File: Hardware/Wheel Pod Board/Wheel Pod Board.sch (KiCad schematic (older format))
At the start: 1 part, among them U1 STM32F401RCT6

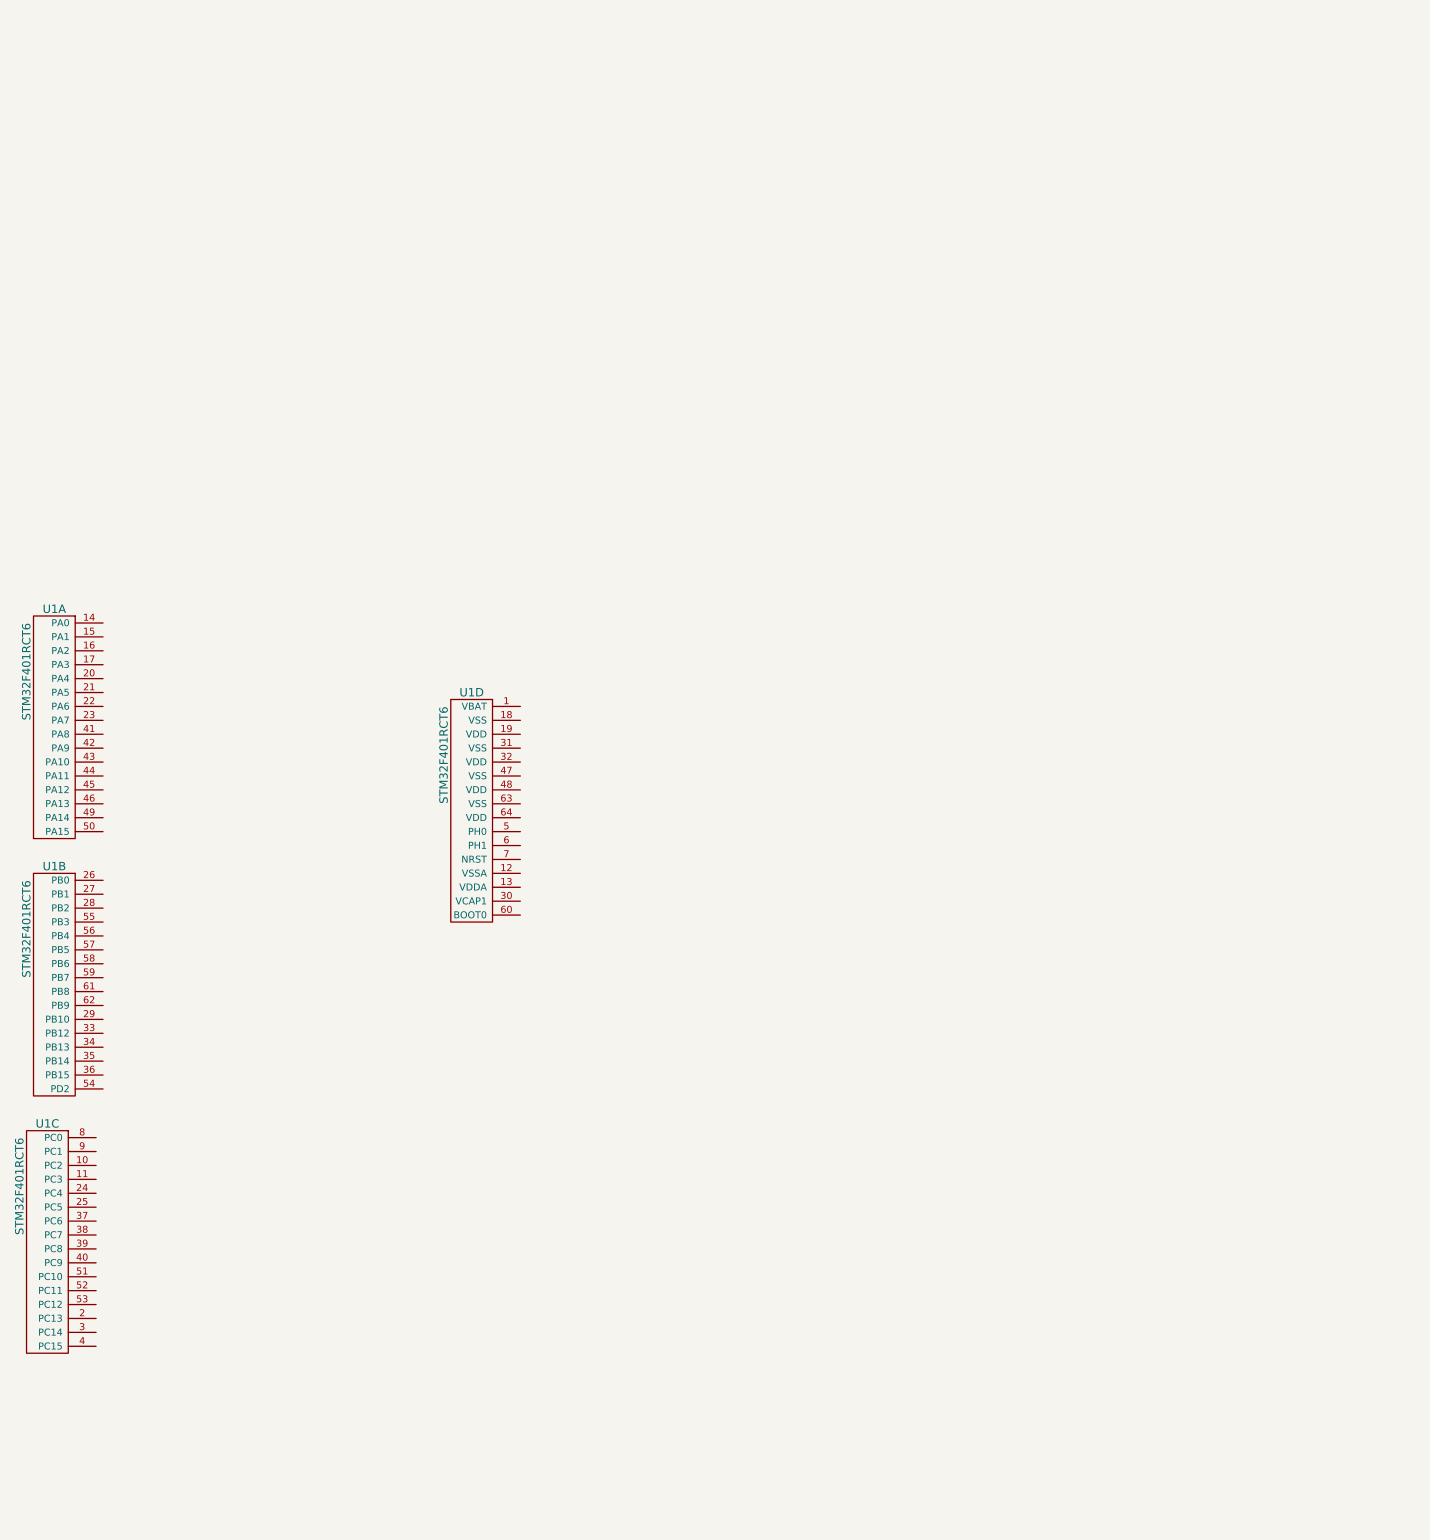
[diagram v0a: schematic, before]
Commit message: Import common blocks from Arm Board
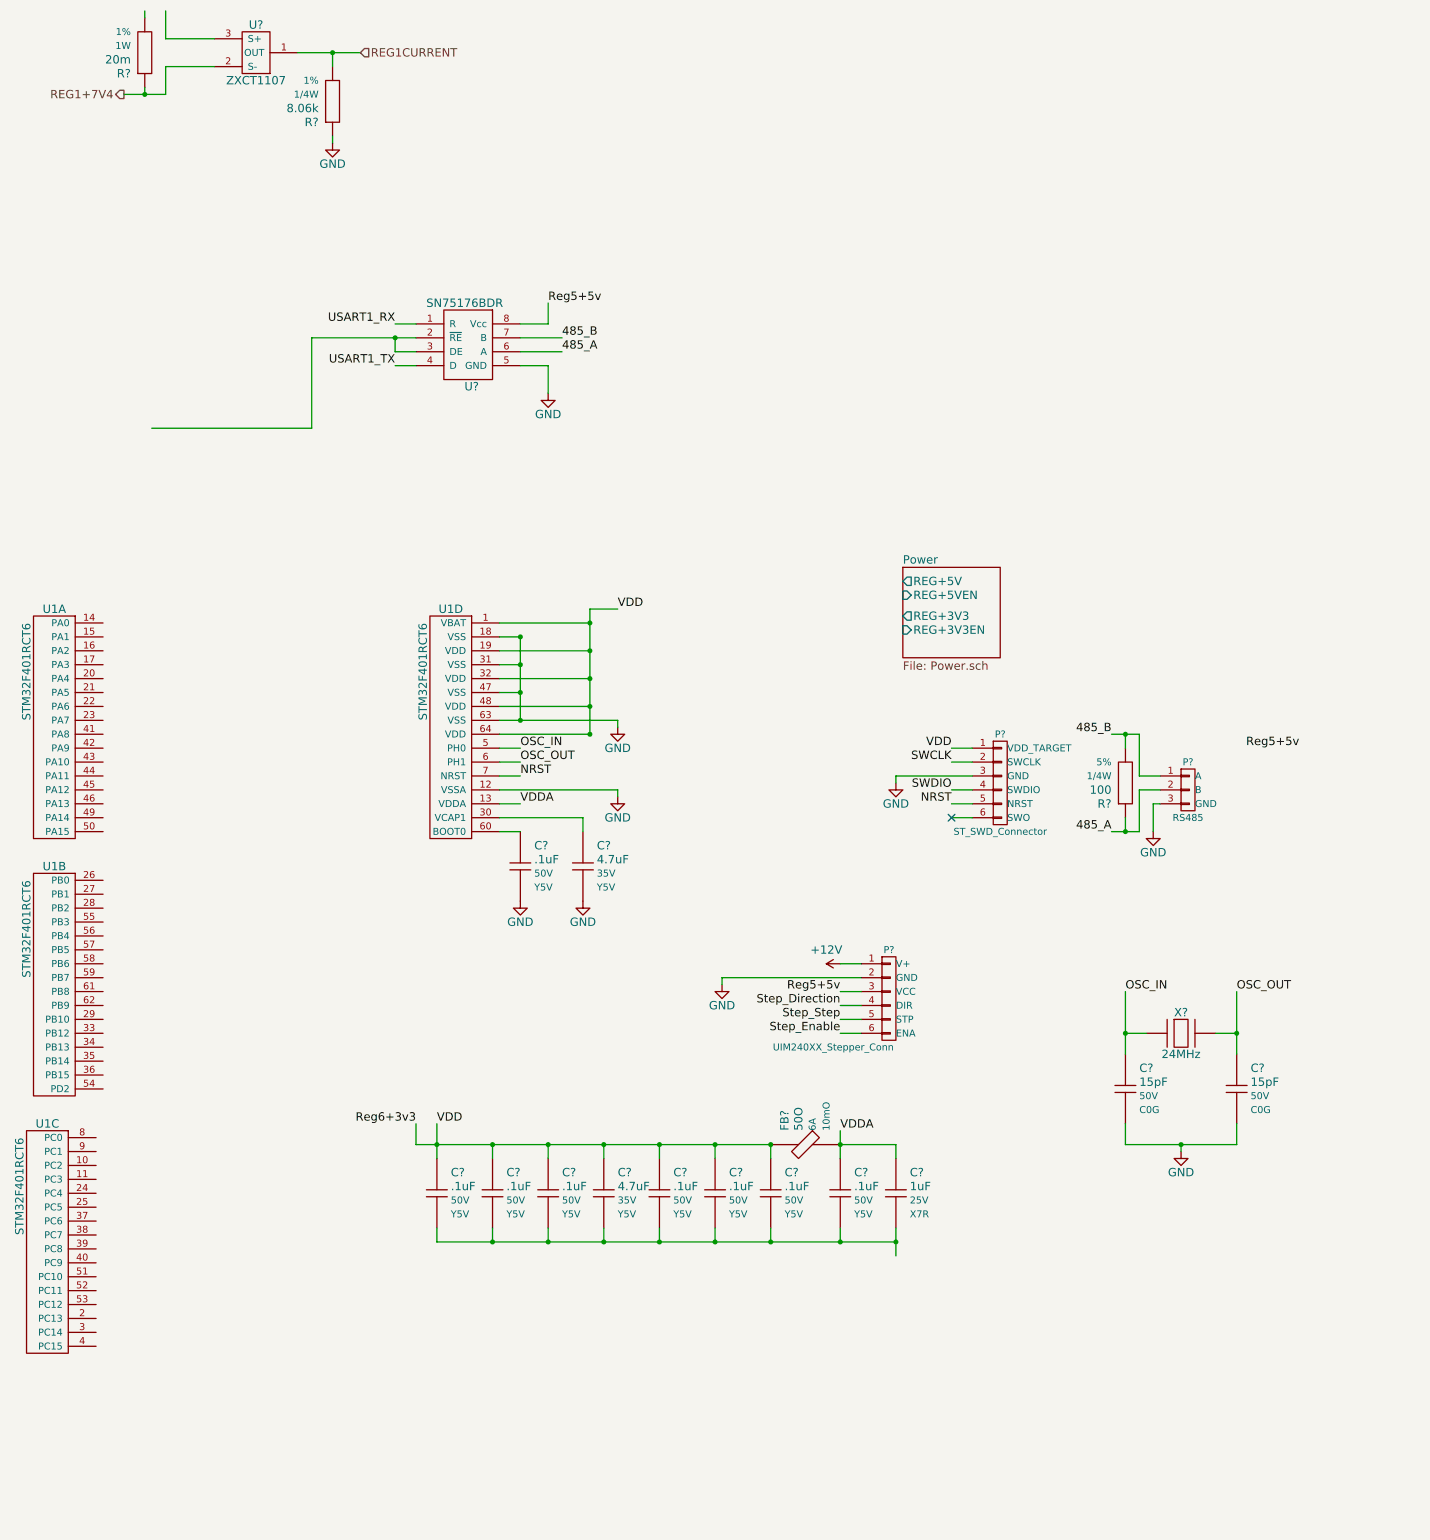
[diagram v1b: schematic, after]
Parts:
- added C? (x2): 4.7uF, Capacitors_SMD:C_1206_HandSoldering, symbol Capacitor
- added C? (x8): .1uF, Capacitors_SMD:C_1206_HandSoldering, symbol Capacitor
- added C?: 1uF, Capacitors_SMD:C_1206_HandSoldering, symbol Capacitor
- added C? (x2): 15pF, Capacitors_SMD:C_1206_HandSoldering, symbol Capacitor
- added FB?: 50O, Resistors_SMD:R_1206_HandSoldering, symbol Ferrite
- added P?: UIM240XX_Stepper_Conn, MAVRIC_footprints:1x6_SMD_header, symbol UIM240XX_Conn
- added P?: RS485, MAVRIC_footprints:1x3_SMD_header, symbol RS485
- added P?: ST_SWD_Connector, MAVRIC_footprints:1x6_SMD_header, symbol ST_SWD_Connector
- added R?: 20m, Resistors_SMD:R_1206_HandSoldering, symbol Resistor
- added R?: 8.06k, Resistors_SMD:R_1206_HandSoldering, symbol Resistor
- added R?: 100, Resistors_SMD:R_1206_HandSoldering, symbol Resistor
- added U?: SN75176BDR, SMD_Packages:SOIC-8-W, symbol SN75176BDR
- added U?: ZXCT1107, Housings_SOT-23_SOT-143_TSOT-6:SOT23_Transistor_Handsoldering_RevB_14Mar2014, symbol ZXCT1107
- added X?: 24MHz, Crystals_Oscillators_SMD:Q_49U3HMS, symbol Crystal
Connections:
- net labels added: +12V, 485_A, 485_B, GND, NRST, OSC_IN, OSC_OUT, REG1+7V4, REG1CURRENT, Reg5+5v, Reg6+3v3, SWCLK, SWDIO, Step_Direction, Step_Enable, Step_Step, USART1_RX, USART1_TX, VDD, VDDA
- wire segments 0 -> 99
- no-connect marks 0 -> 1
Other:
- moved on the sheet: U1D

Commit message: Connect some power, create STMCube project
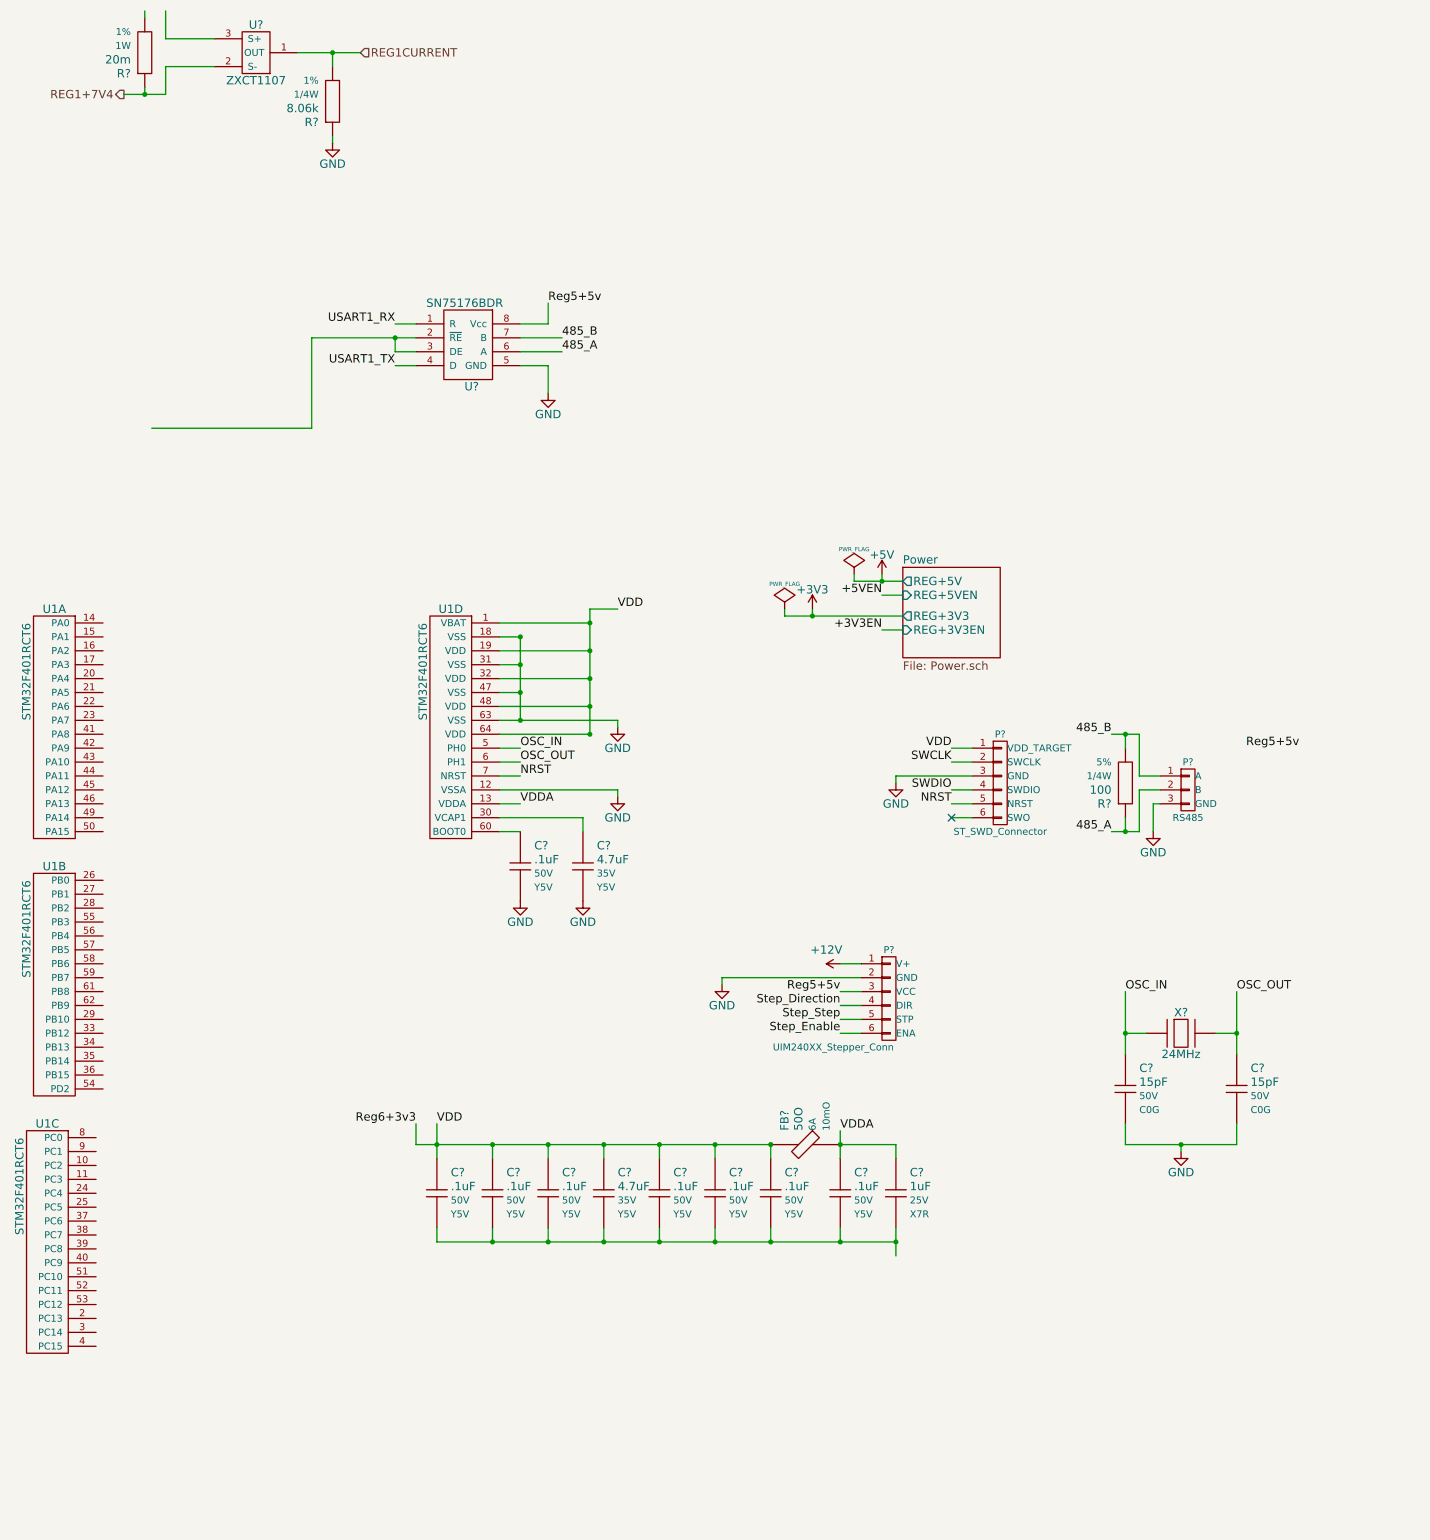
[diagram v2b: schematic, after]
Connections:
- net labels added: +3V3, +3V3EN, +5V, +5VEN
- wire segments 99 -> 140
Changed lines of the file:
@@
 Connection ~ 4650 1450
 Wire Wire Line
-	4500 1850 5350 1850
+	4500 1850 4650 1850
+Wire Wire Line
+	4650 1850 5350 1850
 Connection ~ 4650 1850
 Wire Wire Line
@@
 Connection ~ 5150 1150
 Wire Wire Line
-	4650 1250 4650 1850
-Wire Wire Line
-	5150 1050 5150 1950
+	4650 1250 4650 1450
+Wire Wire Line
+	4650 1450 4650 1650
+Wire Wire Line
+	4650 1650 4650 1850
+Wire Wire Line
+	5150 1050 5150 1150
+Wire Wire Line
+	5150 1150 5150 1350
+Wire Wire Line
+	5150 1350 5150 1550
+Wire Wire Line
+	5150 1550 5150 1750
+Wire Wire Line
+	5150 1750 5150 1950
 Wire Wire Line
 	4500 2650 4650 2650
@@
 	3150 -250 2000 -250
 Wire Wire Line
-	3150 -900 3900 -900
+	3150 -900 3750 -900
+Wire Wire Line
+	3750 -900 3900 -900
 Wire Wire Line
 	3900 -700 3750 -700
@@
 	6450 4900 6450 5000
 Wire Wire Line
-	4050 4750 4050 5000
+	4050 4750 4050 4900
+Wire Wire Line
+	4050 4900 4050 5000
 Connection ~ 4050 4900
 Wire Wire Line
@@
 Connection ~ 6450 5600
 Wire Wire Line
-	6950 4800 6950 5000
+	6950 4800 6950 4900
+Wire Wire Line
+	6950 4900 6950 5000
 Connection ~ 6450 4900
 Connection ~ 6950 4900
@@
 	7350 4900 7350 5000
 Wire Wire Line
-	7350 5500 7350 5700
+	7350 5500 7350 5600
+Wire Wire Line
+	7350 5600 7350 5700
 Wire Wire Line
 	6950 5600 6950 5500
@@
 	6950 4900 7350 4900
 Wire Wire Line
-	4050 5600 7350 5600
-Wire Wire Line
-	3900 4900 6450 4900
+	4050 5600 4450 5600
+Wire Wire Line
+	4450 5600 4850 5600
+Wire Wire Line
+	4850 5600 5250 5600
+Wire Wire Line
+	5250 5600 5650 5600
+Wire Wire Line
+	5650 5600 6050 5600
+Wire Wire Line
+	6050 5600 6450 5600
+Wire Wire Line
+	6450 5600 6950 5600
+Wire Wire Line
+	6950 5600 7350 5600
+Wire Wire Line
+	3900 4900 4050 4900
+Wire Wire Line
+	4050 4900 4450 4900
+Wire Wire Line
+	4450 4900 4850 4900
+Wire Wire Line
+	4850 4900 5250 4900
+Wire Wire Line
+	5250 4900 5650 4900
+Wire Wire Line
+	5650 4900 6050 4900
+Wire Wire Line
+	6050 4900 6450 4900
 Wire Wire Line
 	3900 4750 3900 4900
@@
 	9100 2350 9100 2650
 Wire Wire Line
-	9100 2650 8900 2650
-Wire Wire Line
-	8900 1950 9100 1950
+	9100 2650 9000 2650
+Wire Wire Line
+	9000 2650 8900 2650
+Wire Wire Line
+	8900 1950 9000 1950
+Wire Wire Line
+	9000 1950 9100 1950
 Wire Wire Line
 	9100 1950 9100 2250
@@
 OSC_OUT
 Wire Wire Line
-	9000 3800 9000 4250
+	9000 3800 9000 4100
+Wire Wire Line
+	9000 4100 9000 4250
 Wire Wire Line
 	9000 4100 9150 4100
@@
 	9650 4100 9800 4100
 Wire Wire Line
-	9800 3800 9800 4250
+	9800 3800 9800 4100
+Wire Wire Line
+	9800 4100 9800 4250
 Wire Wire Line
 	9000 4750 9000 4900
 Wire Wire Line
-	9000 4900 9800 4900
+	9000 4900 9400 4900
+Wire Wire Line
+	9400 4900 9800 4900
 Wire Wire Line
 	9800 4900 9800 4750
@@
 	2100 -2850 2450 -2850
 Wire Wire Line
-	3050 -2950 3500 -2950
+	3050 -2950 3300 -2950
+Wire Wire Line
+	3300 -2950 3500 -2950
 Wire Wire Line
 	3300 -2850 3300 -2950
@@
 	1950 -3250 1950 -3200
 Wire Wire Line
-	1800 -2650 2100 -2650
+	1800 -2650 1950 -2650
+Wire Wire Line
+	1950 -2650 2100 -2650
 Wire Wire Line
 	1950 -2700 1950 -2650
@@
 F5 "REG+3V3" O L 7400 1100 60
 $EndSheet
+$Comp
+L +3V3 #PWR?
+U 1 1 54F898ED
+P 6750 1050
+F 0 "#PWR?" H 6750 900 60  0001 C CNN
+F 1 "+3V3" H 6750 1190 60  0000 C CNN
+F 2 "" H 6750 1050 60  0000 C CNN
+F 3 "" H 6750 1050 60  0000 C CNN
+	1    6750 1050
+	1    0    0    -1
+$EndComp
+Wire Wire Line
+	6550 1100 6750 1100
+Wire Wire Line
+	6750 1100 7400 1100
+Wire Wire Line
+	6750 1100 6750 1050
+$Comp
+L PWR_FLAG #FLG?
+U 1 1 54F89ADE
+P 6550 1050
+F 0 "#FLG?" H 6550 1145 30  0001 C CNN
+F 1 "PWR_FLAG" H 6550 1230 30  0000 C CNN
+F 2 "" H 6550 1050 60  0000 C CNN
+F 3 "" H 6550 1050 60  0000 C CNN
+	1    6550 1050
+	1    0    0    -1
+$EndComp
+$Comp
+L +5V #PWR?
+U 1 1 54F89B19
+P 7250 800
+F 0 "#PWR?" H 7250 650 60  0001 C CNN
+F 1 "+5V" H 7250 940 60  0000 C CNN
+F 2 "" H 7250 800 60  0000 C CNN
+F 3 "" H 7250 800 60  0000 C CNN
+	1    7250 800
+	1    0    0    -1
+$EndComp
+Wire Wire Line
+	7250 850  7250 800
+$Comp
+L PWR_FLAG #FLG?
+U 1 1 54F89D36
+P 7050 800
+F 0 "#FLG?" H 7050 895 30  0001 C CNN
+F 1 "PWR_FLAG" H 7050 980 30  0000 C CNN
+F 2 "" H 7050 800 60  0000 C CNN
+F 3 "" H 7050 800 60  0000 C CNN
+	1    7050 800
+	1    0    0    -1
+$EndComp
+Wire Wire Line
+	7050 850  7250 850
+Wire Wire Line
+	7250 850  7400 850
+Wire Wire Line
+	7050 850  7050 800
+Connection ~ 7250 850
+Wire Wire Line
+	6550 1100 6550 1050
+Connection ~ 6750 1100
+Wire Wire Line
+	7400 1200 7250 1200
+Wire Wire Line
+	7400 950  7250 950
+Text Label 7250 950  2    60   ~ 0
++5VEN
+Text Label 7250 1200 2    60   ~ 0
++3V3EN
 $EndSCHEMATC
